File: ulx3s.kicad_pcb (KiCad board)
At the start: 4 copper layers, 94 x 50.8 mm, 93 parts, among them J4 CONN_02X03, U1 LFE5U-85F-6BG381C, U10 IS25LP128F-JBLE, U3 TLV62569DBV, U4 TLV62569DBV, U5 TLV62569DBV, Y1 FNETHE025

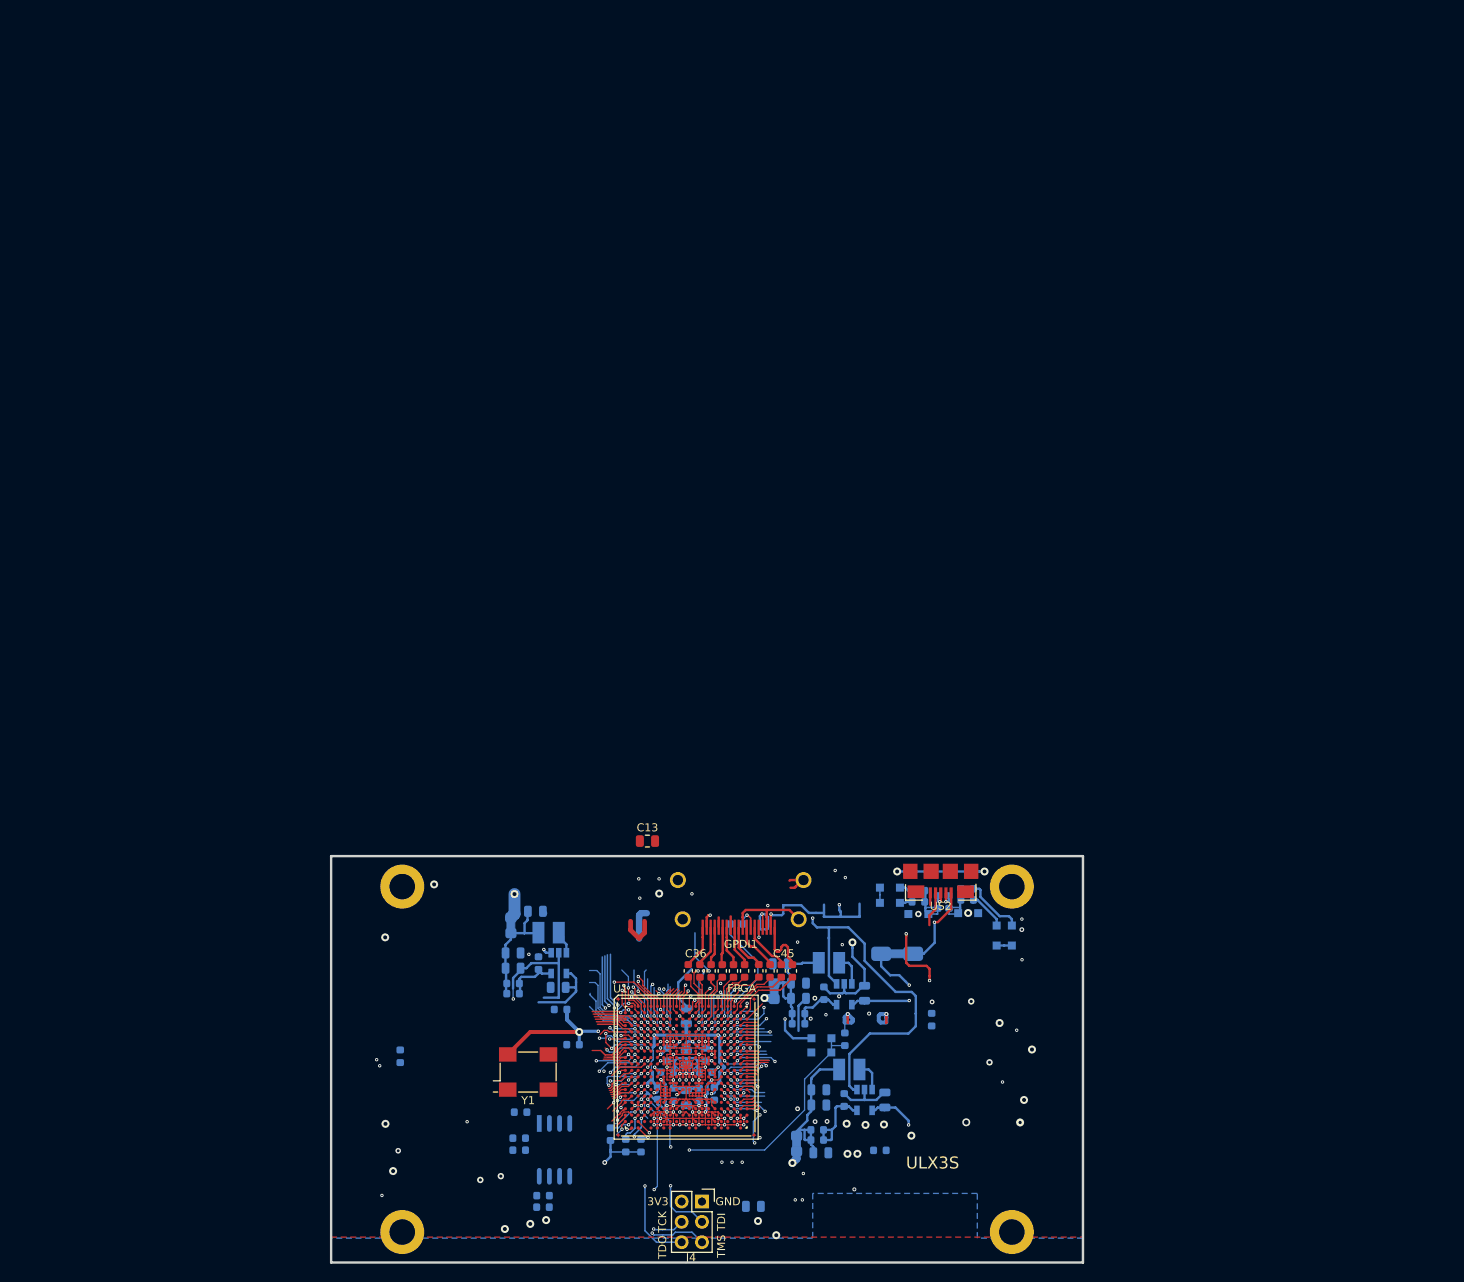
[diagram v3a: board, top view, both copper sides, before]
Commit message: Assigning parts - netlitst to pcb
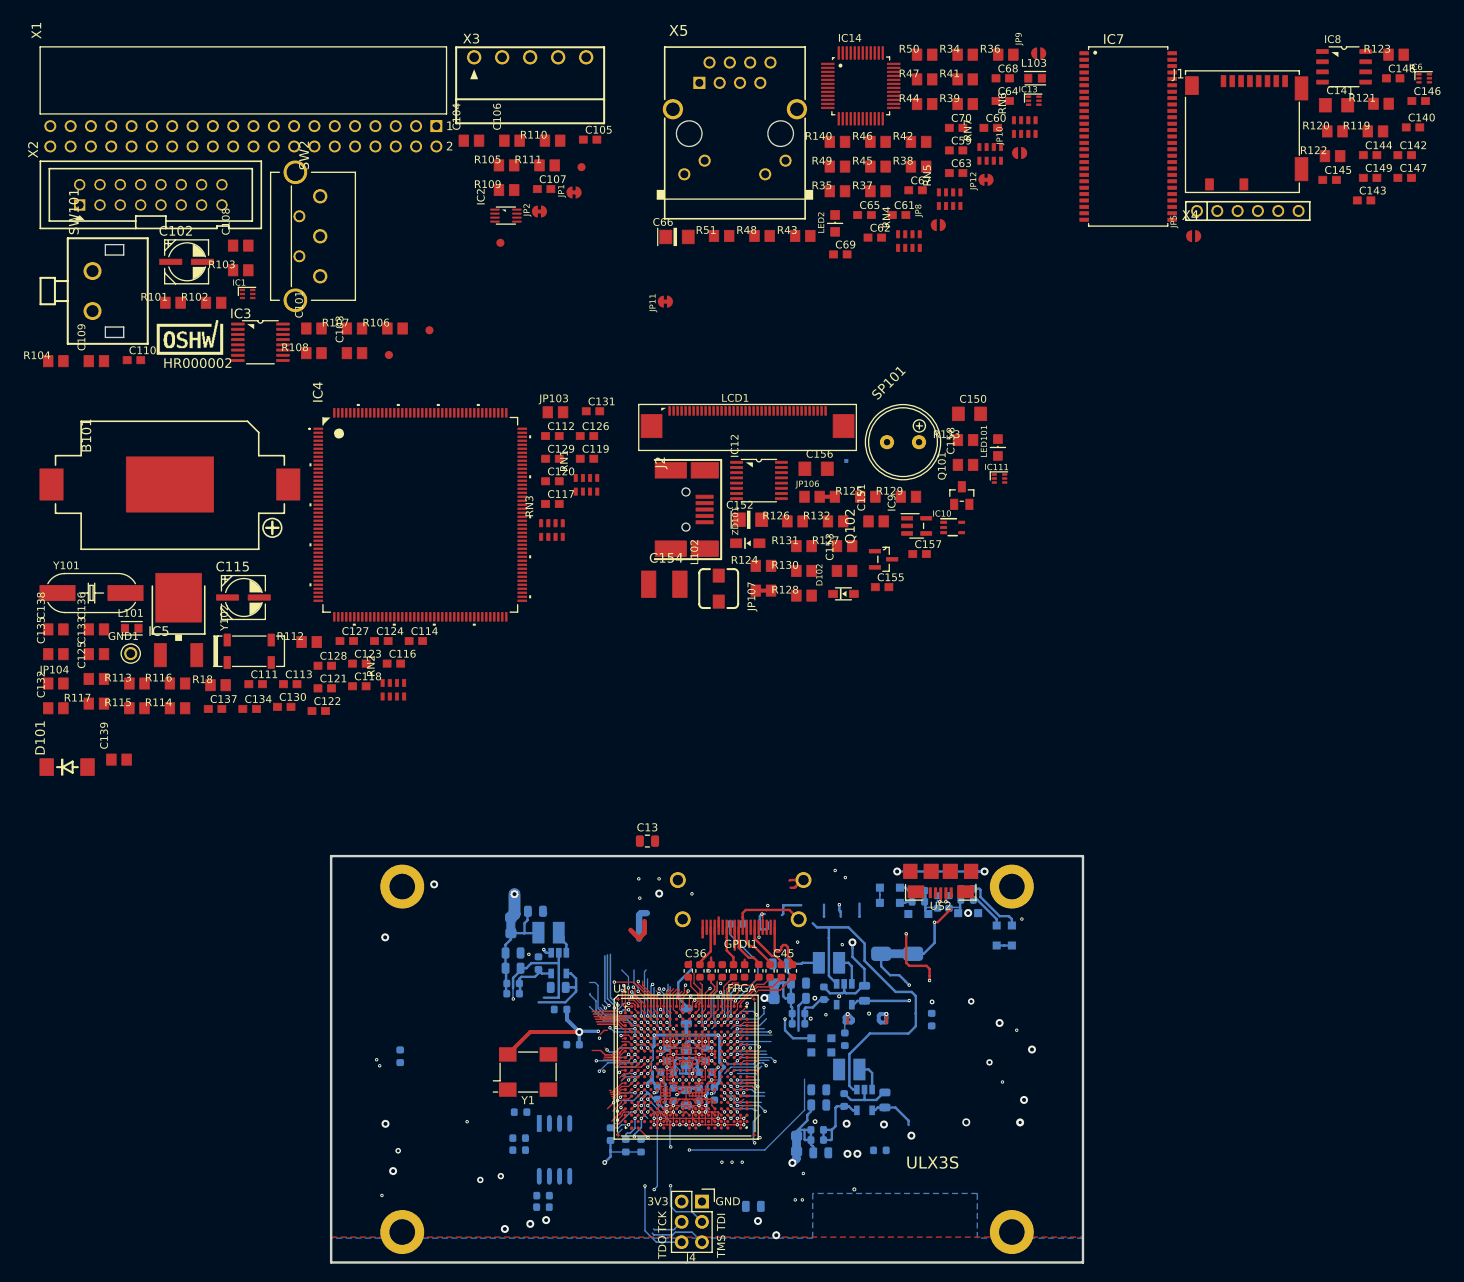
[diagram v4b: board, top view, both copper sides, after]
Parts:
- added B101: DS1092-10-W6L, EEZ DIB MCU r3B4:DS1092-10-W6L, F.Cu at (74.0, 15.0)
- added C101: N.C., EEZ DIB MCU r3B4:C0805, F.Cu at (91.9, -4.53)
- added C102: EEEFK1V220R, EEZ DIB MCU r3B4:PANASONIC_C, F.Cu at (76.0, -12.9)
- added C103: 2u2, EEZ DIB MCU r3B4:C0805, F.Cu at (97.0, -1.44)
- added C104: 10n, EEZ DIB MCU r3B4:C0805, F.Cu at (111.6, -28.0)
- added C105: 100n, EEZ DIB MCU r3B4:C0603, F.Cu at (126.5, -28.1)
- added C106: 10n, EEZ DIB MCU r3B4:C0805, F.Cu at (116.7, -28.0)
- added C107: 100n, EEZ DIB MCU r3B4:C0603, F.Cu at (120.7, -22.0)
- added C108: 10n, EEZ DIB MCU r3B4:C0805, F.Cu at (82.8, -14.9)
- added C109: 10n, EEZ DIB MCU r3B4:C0805, F.Cu at (64.8, -0.44)
- added C110: 100n, EEZ DIB MCU r3B4:C0603, F.Cu at (69.5, -0.57)
- added C111: 33p, EEZ DIB MCU r3B4:C0603, F.Cu at (84.7, 39.9)
- added C112: 4p7, EEZ DIB MCU r3B4:C0603, F.Cu at (121.8, 8.91)
- added C113: 33p, EEZ DIB MCU r3B4:C0603, F.Cu at (89.0, 39.9)
- added C114: 4p7, EEZ DIB MCU r3B4:C0603, F.Cu at (104.7, 34.5)
- added C115: EEEFK1V220R, EEZ DIB MCU r3B4:PANASONIC_C, F.Cu at (83.1, 29.1)
- added C116: 100n, EEZ DIB MCU r3B4:C0603, F.Cu at (101.9, 37.4)
- added C117: 100n, EEZ DIB MCU r3B4:C0603, F.Cu at (121.8, 17.4)
- added C118: 100n, EEZ DIB MCU r3B4:C0603, F.Cu at (97.6, 40.2)
- added C119: 100n, EEZ DIB MCU r3B4:C0603, F.Cu at (126.1, 11.7)
- added C120: 100n, EEZ DIB MCU r3B4:C0603, F.Cu at (121.8, 14.6)
- added C121: 100n, EEZ DIB MCU r3B4:C0603, F.Cu at (93.3, 40.4)
- added C122: 100n, EEZ DIB MCU r3B4:C0603, F.Cu at (92.6, 43.3)
- added C123: 100n, EEZ DIB MCU r3B4:C0603, F.Cu at (97.6, 37.4)
- added C124: 100n, EEZ DIB MCU r3B4:C0603, F.Cu at (100.4, 34.5)
- added C125: 1u, EEZ DIB MCU r3B4:C0805, F.Cu at (64.8, 39.3)
- added C126: 100n, EEZ DIB MCU r3B4:C0603, F.Cu at (126.1, 8.91)
- added C127: 100n, EEZ DIB MCU r3B4:C0603, F.Cu at (96.1, 34.5)
- added C128: 100n, EEZ DIB MCU r3B4:C0603, F.Cu at (93.3, 37.6)
- added C129: 100n, EEZ DIB MCU r3B4:C0603, F.Cu at (121.8, 11.7)
- added C130: 100n, EEZ DIB MCU r3B4:C0603, F.Cu at (88.2, 42.8)
- added C131: 100n, EEZ DIB MCU r3B4:C0603, F.Cu at (126.8, 5.82)
- added C132: 2u2, EEZ DIB MCU r3B4:C0805, F.Cu at (59.7, 42.9)
- added C133: 2u2, EEZ DIB MCU r3B4:C0805, F.Cu at (64.8, 36.2)
- added C134: 100n, EEZ DIB MCU r3B4:C0603, F.Cu at (83.9, 43.0)
- added C135: 1u, EEZ DIB MCU r3B4:C0805, F.Cu at (59.7, 36.2)
- added C136: 1u, EEZ DIB MCU r3B4:C0805, F.Cu at (64.8, 33.1)
- added C137: 100n, EEZ DIB MCU r3B4:C0603, F.Cu at (79.6, 43.0)
- added C138: 2u2, EEZ DIB MCU r3B4:C0805, F.Cu at (59.7, 33.1)
- added C139: 2u2, EEZ DIB MCU r3B4:C0805, F.Cu at (67.6, 49.4)
- added C140: N.C., EEZ DIB MCU r3B4:C0603, F.Cu at (229.3, -29.7)
- added C141: 4u7, EEZ DIB MCU r3B4:C1206, F.Cu at (219.8, -32.4)
- added C142: 100n, EEZ DIB MCU r3B4:C0603, F.Cu at (228.3, -26.2)
- added C143: 100n, EEZ DIB MCU r3B4:C0603, F.Cu at (223.2, -20.5)
- added C144: 100n, EEZ DIB MCU r3B4:C0603, F.Cu at (224.0, -26.2)
- added C145: 100n, EEZ DIB MCU r3B4:C0603, F.Cu at (218.9, -23.1)
- added C146: 100n, EEZ DIB MCU r3B4:C0603, F.Cu at (230.0, -33.0)
- added C147: 100n, EEZ DIB MCU r3B4:C0603, F.Cu at (228.3, -23.4)
- added C148: 100n, EEZ DIB MCU r3B4:C0603, F.Cu at (226.9, -35.8)
- added C149: 100n, EEZ DIB MCU r3B4:C0603, F.Cu at (224.0, -23.4)
- added C150: 4u7, EEZ DIB MCU r3B4:C1206, F.Cu at (173.9, 6.14)
- added C151: 1u, EEZ DIB MCU r3B4:C0805, F.Cu at (162.2, 19.6)
- added C152: 4u7, EEZ DIB MCU r3B4:EC1206, F.Cu at (146.5, 19.4)
- added C153: 2u2, EEZ DIB MCU r3B4:C0805, F.Cu at (158.3, 25.8)
- added C154: 4n7/1kV, EEZ DIB MCU r3B4:C1812, F.Cu at (135.7, 27.4)
- added C155: 100n, EEZ DIB MCU r3B4:C0603, F.Cu at (163.0, 27.8)
- added C156: 4u7, EEZ DIB MCU r3B4:C1206, F.Cu at (154.7, 13.0)
- added C157: 100n, EEZ DIB MCU r3B4:C0603, F.Cu at (167.7, 23.7)
- added C158: 1u, EEZ DIB MCU r3B4:C0805, F.Cu at (173.4, 12.5)
- added C59: N.C., EEZ DIB MCU r3B4:C0603, F.Cu at (172.2, -26.8)
- added C60: 100n, EEZ DIB MCU r3B4:C0603, F.Cu at (176.5, -29.6)
- added C61: 100n, EEZ DIB MCU r3B4:C0603, F.Cu at (165.1, -18.7)
- added C62: 100n, EEZ DIB MCU r3B4:C0603, F.Cu at (162.1, -15.9)
- added C63: 100n, EEZ DIB MCU r3B4:C0603, F.Cu at (172.2, -24.0)
- added C64: 100n, EEZ DIB MCU r3B4:C0603, F.Cu at (178.1, -33.0)
- added C65: 100n, EEZ DIB MCU r3B4:C0603, F.Cu at (160.8, -18.7)
- added C66: 10u, EEZ DIB MCU r3B4:EC1206, F.Cu at (137.3, -16.0)
- added C67: 100n, EEZ DIB MCU r3B4:C0603, F.Cu at (167.2, -21.8)
- added C68: 100n, EEZ DIB MCU r3B4:C0603, F.Cu at (178.1, -35.8)
- added C69: 100n, EEZ DIB MCU r3B4:C0603, F.Cu at (157.7, -13.8)
- added C70: 100n, EEZ DIB MCU r3B4:C0603, F.Cu at (172.2, -29.6)
- added D101: SMBJ5.0A-TR, EEZ DIB MCU r3B4:DO214AA, F.Cu at (61.1, 50.3)
- added D102: RB751V40T1G, EEZ DIB MCU r3B4:SOD323-R, F.Cu at (158.1, 28.6)
- added FM1: FIDUCIAL, EEZ DIB MCU r3B4:FIDUCIAL, F.Cu at (125.4, -24.7)
- added FM2: FIDUCIAL, EEZ DIB MCU r3B4:FIDUCIAL, F.Cu at (115.3, -15.2)
- added FM3: FIDUCIAL, EEZ DIB MCU r3B4:FIDUCIAL, F.Cu at (106.4, -4.31)
- added FM4: FIDUCIAL, EEZ DIB MCU r3B4:FIDUCIAL, F.Cu at (101.3, -1.22)
- added GND1: PCB_TEST_TABSHIELD, EEZ DIB MCU r3B4:PCB_SHIELD_TAB, F.Cu at (69.1, 36.1)
- added IC1: TPD4E001DRLR, EEZ DIB MCU r3B4:DRL6, F.Cu at (83.7, -8.85)
- added IC10: TPS61169DCKR, EEZ DIB MCU r3B4:DCK5, F.Cu at (171.8, 20.3)
- added IC111: TPD4E001DRLR, EEZ DIB MCU r3B4:DRL6, F.Cu at (177.6, 14.2)
- added IC12: TSC2007IPW, EEZ DIB MCU r3B4:PW(R-PDSO-G16), F.Cu at (147.6, 14.5)
- added IC13: N.C., EEZ DIB MCU r3B4:DRL6, F.Cu at (181.9, -33.0)
- added IC14: DP83848CVV_NOPB, EEZ DIB MCU r3B4:PT48, F.Cu at (160.3, -34.9)
- added IC2: 74AUP1G74DC.125, EEZ DIB MCU r3B4:DCU8, F.Cu at (115.9, -18.6)
- added IC3: CD74HC4050PWR, EEZ DIB MCU r3B4:PW16, F.Cu at (85.3, -2.81)
- added IC4: STM32F769IIT6, EEZ DIB MCU r3B4:LQFP-176_24X24MM, F.Cu at (105.2, 18.8)
- added IC5: LD1117ADT33TR, EEZ DIB MCU r3B4:DPACK, F.Cu at (75.0, 31.5)
- added IC6: N.C., EEZ DIB MCU r3B4:DRL6, F.Cu at (230.7, -35.8)
- added IC7: IS42S16400J, EEZ DIB MCU r3B4:TSOPII-54, F.Cu at (193.7, -28.5)
- added IC8: AT24C256C-SSHL-B, EEZ DIB MCU r3B4:SOIC127P600X173-8N, F.Cu at (220.7, -37.2)
- added IC9: TPS2051BDBVR, EEZ DIB MCU r3B4:DBV5, F.Cu at (167.3, 20.1)
- added J1: 503398-1892, EEZ DIB MCU r3B4:5033981892, F.Cu at (201.2, -22.8)
- added J2: 67803-8020, EEZ DIB MCU r3B4:678038020, F.Cu at (134.6, 18.1)
- added JP1: JP2-NOCUT, EEZ DIB MCU r3B4:JP2-NOCUT, F.Cu at (124.5, -21.5)
- added JP10: JP2-CUT, EEZ DIB MCU r3B4:JP2-CUT, F.Cu at (180.2, -26.5)
- added JP103: JP2-CUT-0805, EEZ DIB MCU r3B4:R_0805, F.Cu at (122.1, 5.95)
- added JP104: JP2-CUT-0805, EEZ DIB MCU r3B4:R_0805, F.Cu at (59.7, 39.8)
- added JP106: JP3-CUT-0805-ROTATED, EEZ DIB MCU r3B4:JP3-0805-CUT2, F.Cu at (155.2, 16.5)
- added JP107: JP2-NOCUT-0805, EEZ DIB MCU r3B4:JP2-0805-NOCUT, F.Cu at (148.1, 28.2)
- added JP11: JP2-NOCUT, EEZ DIB MCU r3B4:JP2-NOCUT, F.Cu at (135.9, -7.89)
- added JP12: JP2-NOCUT, EEZ DIB MCU r3B4:JP2-NOCUT, F.Cu at (176.0, -23.1)
- added JP2: JP2-NOCUT, EEZ DIB MCU r3B4:JP2-NOCUT, F.Cu at (120.1, -19.2)
- added JP5: JP2-CUT, EEZ DIB MCU r3B4:JP2-CUT, F.Cu at (201.9, -16.1)
- added JP8: JP2-CUT, EEZ DIB MCU r3B4:JP2-CUT, F.Cu at (170.0, -17.5)
- added JP9: JP2-CUT, EEZ DIB MCU r3B4:JP2-CUT, F.Cu at (182.5, -38.9)
- added L101: BLM18AG102SH1D, EEZ DIB MCU r3B4:BEAD0603, F.Cu at (69.2, 32.9)
- added L102: DLG-0403-4R7, EEZ DIB MCU r3B4:DE0403, F.Cu at (142.5, 28.0)
- added L103: BLM18AG102SH1D, EEZ DIB MCU r3B4:BEAD0603, F.Cu at (182.1, -35.8)
- added LABEL1: HR000002, EEZ DIB MCU r3B4:CERT-SMALL-SILK, F.Cu at (76.5, -1.24)
- added LCD1: 505110-4091, EEZ DIB MCU r3B4:FPC_40, F.Cu at (146.2, 7.66)
- added LED101: N.C., EEZ DIB MCU r3B4:LED_0805, F.Cu at (177.4, 10.3)
- added LED2: N.C., EEZ DIB MCU r3B4:LED_0805, F.Cu at (157.1, -17.7)
- added Q101: N.C., EEZ DIB MCU r3B4:SOT23-BEC, F.Cu at (172.9, 16.4)
- added Q102: 2N7002, EEZ DIB MCU r3B4:SOT103P240X110-3N, F.Cu at (163.2, 24.3)
- added R101: 4K7, EEZ DIB MCU r3B4:R0805, F.Cu at (74.3, -7.75)
- added R102: 10K, EEZ DIB MCU r3B4:R0805, F.Cu at (79.4, -7.75)
- added R103: 10K, EEZ DIB MCU r3B4:R0805, F.Cu at (82.8, -11.8)
- added R104: 4K7, EEZ DIB MCU r3B4:R0805, F.Cu at (59.7, -0.44)
- added R105: 4K7, EEZ DIB MCU r3B4:R0805, F.Cu at (116.0, -24.9)
- added R106: 1K, EEZ DIB MCU r3B4:R0805, F.Cu at (102.1, -4.53)
- added R107: 4K7, EEZ DIB MCU r3B4:R0805, F.Cu at (97.0, -4.53)
- added R108: 4K7, EEZ DIB MCU r3B4:R0805, F.Cu at (91.9, -1.44)
- added R109: 4K7, EEZ DIB MCU r3B4:R0805, F.Cu at (116.0, -21.8)
- added R110: 1K, EEZ DIB MCU r3B4:R0805, F.Cu at (121.8, -28.0)
- added R111: 10K, EEZ DIB MCU r3B4:R0805, F.Cu at (121.1, -24.9)
- added R112: 4K7, EEZ DIB MCU r3B4:R0805, F.Cu at (91.4, 34.7)
- added R113: 10K, EEZ DIB MCU r3B4:R0805, F.Cu at (69.8, 39.8)
- added R114: N.C., EEZ DIB MCU r3B4:R0805, F.Cu at (74.9, 42.9)
- added R115: 4K7, EEZ DIB MCU r3B4:R0805, F.Cu at (69.8, 42.9)
- added R116: 1K5, EEZ DIB MCU r3B4:R0805, F.Cu at (74.9, 39.8)
- added R117: 1K5, EEZ DIB MCU r3B4:R0805, F.Cu at (64.8, 42.4)
- added R119: N.C., EEZ DIB MCU r3B4:R0805, F.Cu at (224.6, -29.2)
- added R120: N.C., EEZ DIB MCU r3B4:R0805, F.Cu at (219.6, -29.2)
- added R121: N.C., EEZ DIB MCU r3B4:R0805, F.Cu at (225.3, -32.6)
- added R122: 47K, EEZ DIB MCU r3B4:R0805, F.Cu at (219.3, -26.1)
- added R123: 47K, EEZ DIB MCU r3B4:R0805, F.Cu at (227.2, -38.8)
- added R124: 10R, EEZ DIB MCU r3B4:R0805, F.Cu at (148.1, 25.1)
- added R125: N.C., EEZ DIB MCU r3B4:R0805, F.Cu at (161.2, 16.5)
- added R126: 10R, EEZ DIB MCU r3B4:R0805, F.Cu at (152.1, 19.6)
- added R127: 10K, EEZ DIB MCU r3B4:R0805, F.Cu at (158.3, 22.7)
- added R128: N.C., EEZ DIB MCU r3B4:R0805, F.Cu at (153.2, 28.9)
- added R129: 4K7, EEZ DIB MCU r3B4:R0805, F.Cu at (166.3, 16.5)
- added R130: 22R, EEZ DIB MCU r3B4:R0805, F.Cu at (153.2, 25.8)
- added R131: 22R, EEZ DIB MCU r3B4:R0805, F.Cu at (153.2, 22.7)
- added R132: 10K, EEZ DIB MCU r3B4:R0805, F.Cu at (157.2, 19.6)
- added R133: 10K, EEZ DIB MCU r3B4:R0805, F.Cu at (173.4, 9.42)
- added R140: N.C., EEZ DIB MCU r3B4:R0805, F.Cu at (157.4, -27.9)
- added R18: 47R, EEZ DIB MCU r3B4:R0805, F.Cu at (80.0, 40.1)
- added R34: 1K5, EEZ DIB MCU r3B4:R0805, F.Cu at (173.4, -38.8)
- added R35: 49R9, EEZ DIB MCU r3B4:R0805, F.Cu at (157.4, -21.7)
- added R36: 49R9, EEZ DIB MCU r3B4:R0805, F.Cu at (178.4, -38.8)
- added R37: N.C., EEZ DIB MCU r3B4:R0805, F.Cu at (162.5, -21.7)
- added R38: 2K2, EEZ DIB MCU r3B4:R0805, F.Cu at (167.5, -24.8)
- added R39: 49R9, EEZ DIB MCU r3B4:R0805, F.Cu at (173.4, -32.6)
- added R41: N.C., EEZ DIB MCU r3B4:R0805, F.Cu at (173.4, -35.7)
- added R42: N.C., EEZ DIB MCU r3B4:R0805, F.Cu at (167.5, -27.9)
- added R43: 2K2, EEZ DIB MCU r3B4:R0805, F.Cu at (153.0, -16.1)
- added R44: 49R9, EEZ DIB MCU r3B4:R0805, F.Cu at (168.3, -32.6)
- added R45: 2K2, EEZ DIB MCU r3B4:R0805, F.Cu at (162.5, -24.8)
- added R46: 220R, EEZ DIB MCU r3B4:R0805, F.Cu at (162.5, -27.9)
- added R47: 220R, EEZ DIB MCU r3B4:R0805, F.Cu at (168.3, -35.7)
- added R48: 2K2, EEZ DIB MCU r3B4:R0805, F.Cu at (148.0, -16.1)
- added R49: 2K2, EEZ DIB MCU r3B4:R0805, F.Cu at (157.4, -24.8)
- added R50: 4K87, EEZ DIB MCU r3B4:R0805, F.Cu at (168.3, -38.8)
- added R51: 2K2, EEZ DIB MCU r3B4:R0805, F.Cu at (142.9, -16.1)
- added RN1: DR1206-33R-4/8, EEZ DIB MCU r3B4:CAY16, F.Cu at (126.0, 15.0)
- added RN2: DR1206-33R-4/8, EEZ DIB MCU r3B4:CAY16, F.Cu at (101.9, 40.6)
- added RN3: DR1206-33R-4/8, EEZ DIB MCU r3B4:CAY16, F.Cu at (121.7, 20.7)
- added RN4: DR1206-33R-4/8, EEZ DIB MCU r3B4:CAY16, F.Cu at (166.3, -15.5)
- added RN5: DR1206-33R-4/8, EEZ DIB MCU r3B4:CAY16, F.Cu at (171.4, -20.7)
- added RN6: DR1206-33R-4/8, EEZ DIB MCU r3B4:CAY16, F.Cu at (180.8, -29.7)
- added RN7: DR1206-33R-4/8, EEZ DIB MCU r3B4:CAY16, F.Cu at (176.5, -26.4)
- added SH1: SHORTNOHOLE, EEZ DIB MCU r3B4:SHORT_NOHOLE, F.Cu at (158.5, 12.0)
- added SP101: LD-BZEN 0903, EEZ DIB MCU r3B4:LD-BZEN-0903, F.Cu at (165.6, 9.68)
- added SW101: TL1100CF160Q, EEZ DIB MCU r3B4:TL1100C, F.Cu at (64.3, -9.21)
- added SW2: PEC16-2215F-S0024, EEZ DIB MCU r3B4:PEC16-2215F, F.Cu at (92.7, -16.1)
- added X1: DS1024-2*20R0, EEZ DIB MCU r3B4:ZL263-40DG, F.Cu at (59.0, -27.3)
- added X2: DS1013-16SSIB1, EEZ DIB MCU r3B4:IDC-16PIN, F.Cu at (71.6, -21.2)
- added X3: 691322110005, EEZ DIB MCU r3B4:MC1,5_5-G-3,5, F.Cu at (119.0, -38.4)
- added X4: N.C., EEZ DIB MCU r3B4:SSW-106-02-S-S, F.Cu at (208.7, -19.2)
- added X5: LMJTAB881243M-L, EEZ DIB MCU r3B4:RJ45-TRAFO-LED, F.Cu at (144.6, -28.9)
- added Y101: 25MHz, EEZ DIB MCU r3B4:HC-49_4H, F.Cu at (64.2, 28.5)
- added Y102: XTAL016178-85SMX, EEZ DIB MCU r3B4:85SMX, F.Cu at (83.9, 35.8)
- added ZD101: BZX384-B24.115, EEZ DIB MCU r3B4:SOD323-W, F.Cu at (146.2, 22.3)
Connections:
- net 2V5_3V3 renamed +3V3
- U1 pad G1: /usb/ANT_433MHz -> (no net)
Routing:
- net (no net): track 820.1 -> 692.0 mm, vias 159 -> 141
- net +3V3: track 138.6 -> 80.4 mm, vias 26 -> 16
- net +5V: track 158.3 -> 109.5 mm, vias 7 -> 4
- net 2V5_3V3: track 0.00 -> 41.2 mm, vias 0 -> 8
- net GND: track 278.2 -> 256.1 mm, vias 110 -> 103
- net /gpio/OUT5V: track 24.2 -> 9.69 mm
- net /flash/FPGA_PROGRAMN: track 36.3 -> 26.2 mm, vias 2 -> 1
- net /power/P1V1: track 18.5 -> 11.2 mm
- net USB_FPGA_PULL_D-: track 8.33 -> 2.47 mm, vias 2 -> 1
- net +2V5: track 98.0 -> 92.7 mm, vias 9 -> 8
- net /gpdi/GPDI_D1-: track 4.80 -> 0.11 mm
- net +1V1: track 72.8 -> 68.4 mm
- net USB_FPGA_D-: track 15.8 -> 11.7 mm, vias 3 -> 2
- net SPI2_CLK: track 0.00 -> 4.01 mm
- net /gpdi/GPDI_D2+: track 5.33 -> 1.69 mm
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- added copper zone on In1.Cu, net 2V5_3V3

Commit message: Frame around FPGA
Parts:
- IC7: moved to B.Cu
- moved C65 233.9 mm to (-71.9, 5.56)
- moved C69 233.9 mm to (-74.9, 10.5)
- moved JP8 233.9 mm to (-62.6, 6.82)
- moved R35 233.9 mm to (-75.3, 2.60)
- moved C61 233.9 mm to (-67.5, 5.56)
- moved C62 233.9 mm to (-70.6, 8.39)
- moved C67 233.9 mm to (-65.5, 2.47)
- moved JP12 233.9 mm to (-56.7, 1.16)
- moved LED2 233.9 mm to (-75.5, 6.61)
- moved R37 233.9 mm to (-70.2, 2.60)
- moved RN4 233.9 mm to (-66.3, 8.82)
- moved RN5 233.9 mm to (-61.2, 3.58)
- moved R140 233.1 mm to (-74.6, -5.69)
- moved R49 233.1 mm to (-74.6, -2.60)
- moved RN7 233.1 mm to (-55.5, -4.19)
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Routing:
- net +5V: track 109.5 -> 35.7 mm, vias 4 -> 1
- net (no net): track 692.0 -> 669.4 mm, vias 141 -> 138
- net GND: track 256.1 -> 241.1 mm, vias 103 -> 82
- net JTAG_TMS: track 23.2 -> 11.0 mm, vias 1 -> 2
- net JTAG_TDO: track 20.7 -> 9.95 mm
- net JTAG_TCK: track 20.6 -> 11.8 mm
- net JTAG_TDI: track 19.9 -> 12.6 mm
- net /gpio/IN5V: track 26.1 -> 18.9 mm, vias 1 -> 0
- net /usb/US2VBUS: track 9.52 -> 2.69 mm
- net /gpdi/GPDI_ETH-: track 7.58 -> 1.12 mm
- net /gpdi/GPDI_CLK-: track 6.23 -> 0.20 mm
- net /gpdi/GPDI_ETH+: track 6.27 -> 0.36 mm
- net /gpdi/GPDI_CLK+: track 6.37 -> 0.51 mm
- net /gpio/OUT5V: track 9.69 -> 4.31 mm, vias 2 -> 1
- net /gpdi/FPDI_CEC: track 13.0 -> 7.99 mm
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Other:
- board size 94 x 50.8 mm -> 139.6 x 70.1 mm
- board text removed: "U8"

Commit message: Moving around
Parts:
- removed H1, H2, H3, H4: HOLE, Mounting_Holes:MountingHole_3.2mm_M3_ISO14580_Pad
- C140, C141, C142, C143, C144, C145, C146, C147, C148, C149, IC6, IC8, J1, JP5, R115, R119, R120, R121, R122, R123, X4: moved to B.Cu
- moved RN7 213.9 mm to (154.2, 37.7)
- moved B101 201.6 mm to (202.8, 68.2)
- moved C59 199.4 mm to (128.9, 59.6)
- moved C63 199.4 mm to (128.9, 62.5)
- moved C65 199.4 mm to (116.9, 69.8)
- moved C66 199.4 mm to (116.1, 78.5)
- moved C69 199.4 mm to (113.8, 74.8)
- moved C70 199.4 mm to (128.9, 56.8)
- moved IC14 199.4 mm to (117.0, 51.6)
- moved IC7 199.4 mm to (174.9, 29.4)
- moved J2 199.4 mm to (175.9, 111.5)
- moved JP8 199.4 mm to (126.1, 71.1)
- moved R140 199.4 mm to (114.1, 58.6)
- moved R35 199.4 mm to (113.5, 66.9)
- moved R38 199.4 mm to (124.2, 61.7)
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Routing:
- net +3V3: track 80.4 -> 88.4 mm
- net 2V5_3V3: track 36.3 -> 28.2 mm
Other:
- board size 139.6 x 70.1 mm -> 139.6 x 119.6 mm

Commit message: New annotation - All STM32 parts are +100
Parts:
- moved C119 157.4 mm to (78.1, -59.9)
- moved C129 157.4 mm to (73.8, -59.9)
- moved C133 157.4 mm to (79.8, -130.7)
- moved C135 157.4 mm to (74.7, -130.7)
- moved C7 157.4 mm to (150.3, -94.8)
- moved D21 157.4 mm to (183.5, -154.0)
- moved D23 157.4 mm to (172.4, -152.5)
- moved D24 157.4 mm to (172.4, -154.4)
- moved FM2 157.4 mm to (111.8, -135.4)
- moved IC12 157.4 mm to (180.9, -128.0)
- moved IC6 157.4 mm to (148.3, -49.2)
- moved IC7 157.4 mm to (148.8, -125.8)
- moved JP106 157.4 mm to (188.5, -126.0)
- moved R109 157.4 mm to (112.5, -142.0)
- moved R117 157.4 mm to (166.6, -130.9)
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
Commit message: All STM32 parts are now +100, moving parts to original position
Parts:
- removed C59: N.C., EEZ DIB MCU r3B4:C0603
- removed C60, C61, C62, C63, C64, C65, C67, C68, C69, C70: 100n, EEZ DIB MCU r3B4:C0603
- removed C66: 10u, EEZ DIB MCU r3B4:EC1206
- removed IC13: N.C., EEZ DIB MCU r3B4:DRL6
- removed IC14: DP83848CVV_NOPB, EEZ DIB MCU r3B4:PT48
- removed IC4: STM32F769IIT6, EEZ DIB MCU r3B4:LQFP-176_24X24MM
- removed IC5: LD1117ADT33TR, EEZ DIB MCU r3B4:DPACK
- removed JP10, JP8, JP9: JP2-CUT, EEZ DIB MCU r3B4:JP2-CUT
- removed JP11, JP12: JP2-NOCUT, EEZ DIB MCU r3B4:JP2-NOCUT
- removed LED2: N.C., EEZ DIB MCU r3B4:LED_0805
- removed R18: 47R, EEZ DIB MCU r3B4:R0805
- removed R34: 1K5, EEZ DIB MCU r3B4:R0805
- removed R35, R36, R39, R44: 49R9, EEZ DIB MCU r3B4:R0805
- removed R37, R41, R42: N.C., EEZ DIB MCU r3B4:R0805
- removed R38, R43, R45, R48, R49, R51: 2K2, EEZ DIB MCU r3B4:R0805
- removed R46, R47: 220R, EEZ DIB MCU r3B4:R0805
- removed R50: 4K87, EEZ DIB MCU r3B4:R0805
- removed X4: N.C., EEZ DIB MCU r3B4:SSW-106-02-S-S
- removed X5: LMJTAB881243M-L, EEZ DIB MCU r3B4:RJ45-TRAFO-LED
- added C159: N.C., EEZ DIB MCU r3B4:C0603, F.Cu at (99.8, 94.8)
- added C160: 100n, EEZ DIB MCU r3B4:C0603, F.Cu at (100.5, 98.6)
- added C161: 100n, EEZ DIB MCU r3B4:C0603, F.Cu at (98.7, 92.8)
- added C162: 100n, EEZ DIB MCU r3B4:C0603, F.Cu at (106.1, 98.6)
- added C163: 100n, EEZ DIB MCU r3B4:C0603, F.Cu at (107.2, 93.0)
- added C164: 100n, EEZ DIB MCU r3B4:C0603, F.Cu at (100.7, 114.6)
- added C165: 100n, EEZ DIB MCU r3B4:C0603, F.Cu at (94.8, 100.1)
- added C166: 10u, EEZ DIB MCU r3B4:EC1206, F.Cu at (93.6, 108.7)
- added C167: 100n, EEZ DIB MCU r3B4:C0603, F.Cu at (93.5, 105.4)
- added C168: 100n, EEZ DIB MCU r3B4:C0603, F.Cu at (93.5, 103.7)
- added C169: 100n, EEZ DIB MCU r3B4:C0603, F.Cu at (98.5, 114.6)
- added C170: 100n, EEZ DIB MCU r3B4:C0603, F.Cu at (108.5, 109.0)
- added IC104: STM32F769IIT6, EEZ DIB MCU r3B4:LQFP-176_24X24MM, F.Cu at (147.3, 97.3)
- added IC105: LD1117ADT33TR, EEZ DIB MCU r3B4:DPACK, F.Cu at (97.1, 131.7)
- added IC113: N.C., EEZ DIB MCU r3B4:DRL6, F.Cu at (102.6, 93.4)
- added IC114: DP83848CVV_NOPB, EEZ DIB MCU r3B4:PT48, F.Cu at (100.9, 107.2)
- added JP108: JP2-CUT, EEZ DIB MCU r3B4:JP2-CUT, F.Cu at (103.8, 118.5)
- added JP109: JP2-CUT, EEZ DIB MCU r3B4:JP2-CUT, F.Cu at (105.8, 118.5)
- added JP110: JP2-CUT, EEZ DIB MCU r3B4:JP2-CUT, F.Cu at (101.9, 118.5)
- added JP111: JP2-NOCUT, EEZ DIB MCU r3B4:JP2-NOCUT, F.Cu at (107.8, 118.5)
- added JP112: JP2-NOCUT, EEZ DIB MCU r3B4:JP2-NOCUT, F.Cu at (108.2, 99.7)
- added LED102: N.C., EEZ DIB MCU r3B4:LED_0805, F.Cu at (115.8, 83.3)
- added R118: 47R, EEZ DIB MCU r3B4:R0805, F.Cu at (137.5, 81.0)
- added R134: 1K5, EEZ DIB MCU r3B4:R0805, F.Cu at (96.7, 116.9)
- added R135: 49R9, EEZ DIB MCU r3B4:R0805, F.Cu at (96.7, 99.0)
- added R136: 49R9, EEZ DIB MCU r3B4:R0805, F.Cu at (98.6, 99.0)
- added R137: N.C., EEZ DIB MCU r3B4:R0805, F.Cu at (106.7, 120.8)
- added R138: 2K2, EEZ DIB MCU r3B4:R0805, F.Cu at (90.7, 116.9)
- added R139: 49R9, EEZ DIB MCU r3B4:R0805, F.Cu at (102.3, 99.0)
- added R141: N.C., EEZ DIB MCU r3B4:R0805, F.Cu at (115.8, 85.3)
- added R142: N.C., EEZ DIB MCU r3B4:R0805, F.Cu at (98.8, 120.8)
- added R143: 2K2, EEZ DIB MCU r3B4:R0805, F.Cu at (92.7, 116.9)
- added R144: 49R9, EEZ DIB MCU r3B4:R0805, F.Cu at (104.3, 99.0)
- added R145: 2K2, EEZ DIB MCU r3B4:R0805, F.Cu at (94.7, 116.9)
- added R146: 220R, EEZ DIB MCU r3B4:R0805, F.Cu at (115.8, 79.4)
- added R147: 220R, EEZ DIB MCU r3B4:R0805, F.Cu at (115.8, 81.4)
- added R148: 2K2, EEZ DIB MCU r3B4:R0805, F.Cu at (92.9, 94.0)
- added R149: 2K2, EEZ DIB MCU r3B4:R0805, F.Cu at (94.9, 94.0)
- added R150: 4K87, EEZ DIB MCU r3B4:R0805, F.Cu at (92.1, 112.4)
- added R151: 2K2, EEZ DIB MCU r3B4:R0805, F.Cu at (108.2, 96.4)
- added X104: N.C., EEZ DIB MCU r3B4:SSW-106-02-S-S, F.Cu at (172.2, 77.0)
- added X105: LMJTAB881243M-L, EEZ DIB MCU r3B4:RJ45-TRAFO-LED, F.Cu at (102.6, 80.9)
- IC112: renamed from IC12; moved to B.Cu
- R115: moved to F.Cu
- moved C104 292.2 mm to (206.1, 127.1), turned to 180 degrees
- moved FM1 287.3 mm to (214.8, 127.0)
- moved C106 280.0 mm to (186.4, 122.2), turned to 270 degrees
- moved R111 276.9 mm to (190.3, 122.2), turned to 270 degrees
- moved IC102 274.1 mm to (196.5, 122.1), turned to 90 degrees
- moved C105 273.8 mm to (120.7, 125.5)
- moved R114 269.3 mm to (199.2, 122.2), turned to 90 degrees
- moved FM2 269.1 mm to (81.8, 132.0)
- moved JP104 268.7 mm to (193.4, 114.1)
- moved JP106 264.7 mm to (134.8, 133.2), turned to 180 degrees
- moved R105 264.6 mm to (115.5, 119.5), turned to 90 degrees
- moved R109 261.6 mm to (118.0, 119.5), turned to 90 degrees
- moved C115 261.3 mm to (90.1, 123.4), turned to 90 degrees
- moved C138 261.0 mm to (158.3, 113.4), turned to 270 degrees
- moved C107 260.5 mm to (120.2, 118.4), turned to 270 degrees
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- renumbered IC1 to IC101, IC2 to IC102, IC3 to IC103, IC6 to IC106, IC7 to IC107, IC8 to IC108, IC9 to IC109, IC10 to IC110, J1 to J101, J2 to J102, JP1 to JP101, JP2 to JP102, JP5 to JP105, LCD1 to LCD101, SH1 to SH101, SW2 to SW102, X1 to X101, X2 to X102, X3 to X103
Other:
- outline, holes or cut-outs redrawn
